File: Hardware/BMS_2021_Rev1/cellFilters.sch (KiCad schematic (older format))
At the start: 14 parts

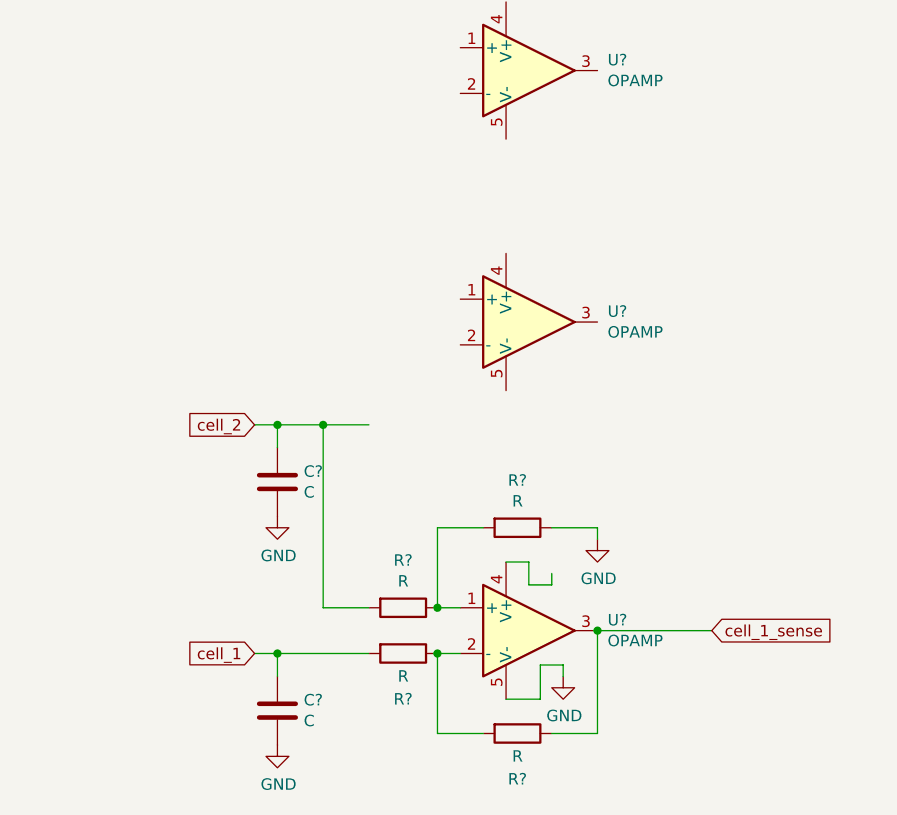
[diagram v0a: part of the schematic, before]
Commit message: Cell filter design finished
need to add resistor values. diodes?
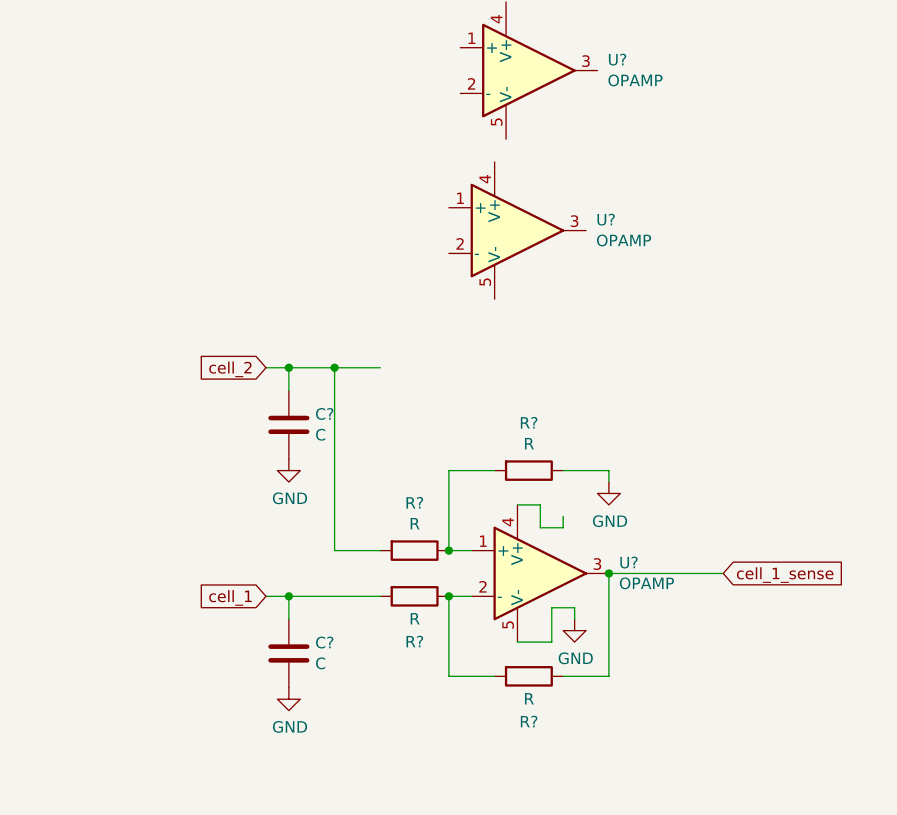
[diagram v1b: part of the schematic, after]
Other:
- moved on the sheet: C?, R?, U?
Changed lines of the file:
@@
 $Descr A4 11693 8268
 encoding utf-8
-Sheet 2 2
+Sheet 2 3
 Title ""
 Date ""
@@
 L pspice:OPAMP U?
 U 1 1 5F757117
-P 8600 4450
-F 0 "U?" H 8944 4496 50  0000 L CNN
-F 1 "OPAMP" H 8944 4405 50  0000 L CNN
-F 2 "" H 8600 4450 50  0001 C CNN
-F 3 "~" H 8600 4450 50  0001 C CNN
-	1    8600 4450
+P 8550 4050
+F 0 "U?" H 8894 4096 50  0000 L CNN
+F 1 "OPAMP" H 8894 4005 50  0000 L CNN
+F 2 "" H 8550 4050 50  0001 C CNN
+F 3 "~" H 8550 4050 50  0001 C CNN
+	1    8550 4050
 	1    0    0    -1
 $EndComp
@@
 L pspice:OPAMP U?
 U 1 1 5F75711D
-P 8600 5800
-F 0 "U?" H 8944 5846 50  0000 L CNN
-F 1 "OPAMP" H 8944 5755 50  0000 L CNN
-F 2 "" H 8600 5800 50  0001 C CNN
-F 3 "~" H 8600 5800 50  0001 C CNN
-	1    8600 5800
-	1    0    0    -1
-$EndComp
-Text GLabel 7400 5900 0    50   Input ~ 0
+P 8650 5550
+F 0 "U?" H 8994 5596 50  0000 L CNN
+F 1 "OPAMP" H 8994 5505 50  0000 L CNN
+F 2 "" H 8650 5550 50  0001 C CNN
+F 3 "~" H 8650 5550 50  0001 C CNN
+	1    8650 5550
+	1    0    0    -1
+$EndComp
+Text GLabel 7450 5650 0    50   Input ~ 0
 cell_1
 $Comp
 L Device:C C?
 U 1 1 5F76C0D8
-P 7500 6150
-F 0 "C?" H 7615 6196 50  0000 L CNN
-F 1 "C" H 7615 6105 50  0000 L CNN
-F 2 "" H 7538 6000 50  0001 C CNN
-F 3 "~" H 7500 6150 50  0001 C CNN
-	1    7500 6150
+P 7550 5900
+F 0 "C?" H 7665 5946 50  0000 L CNN
+F 1 "C" H 7665 5855 50  0000 L CNN
+F 2 "" H 7588 5750 50  0001 C CNN
+F 3 "~" H 7550 5900 50  0001 C CNN
+	1    7550 5900
 	1    0    0    -1
 $EndComp
@@
 L Device:R R?
 U 1 1 5F76C9A3
-P 8050 5900
-F 0 "R?" V 8250 5900 50  0000 C CNN
-F 1 "R" V 8150 5900 50  0000 C CNN
-F 2 "" V 7980 5900 50  0001 C CNN
-F 3 "~" H 8050 5900 50  0001 C CNN
-	1    8050 5900
-	0    1    1    0
-$EndComp
-Wire Wire Line
-	7400 5900 7500 5900
-Wire Wire Line
-	7500 5900 7500 6000
-Wire Wire Line
-	7500 5900 7900 5900
-Connection ~ 7500 5900
-Wire Wire Line
-	8200 5900 8300 5900
-Wire Wire Line
-	8200 5900 8200 6250
-Wire Wire Line
-	8200 6250 8400 6250
-Wire Wire Line
-	8900 6250 8900 5800
-Connection ~ 8200 5900
-Wire Wire Line
-	8900 5800 9400 5800
+P 8100 5650
+F 0 "R?" V 8300 5650 50  0000 C CNN
+F 1 "R" V 8200 5650 50  0000 C CNN
+F 2 "" V 8030 5650 50  0001 C CNN
+F 3 "~" H 8100 5650 50  0001 C CNN
+	1    8100 5650
+	0    1    1    0
+$EndComp
+Wire Wire Line
+	7450 5650 7550 5650
+Wire Wire Line
+	7550 5650 7550 5750
+Wire Wire Line
+	7550 5650 7950 5650
+Connection ~ 7550 5650
+Wire Wire Line
+	8250 5650 8350 5650
+Wire Wire Line
+	8250 5650 8250 6000
+Wire Wire Line
+	8250 6000 8450 6000
+Wire Wire Line
+	8950 6000 8950 5550
+Connection ~ 8250 5650
+Wire Wire Line
+	8950 5550 9450 5550
 $Comp
 L Device:R R?
 U 1 1 5F76FD0D
-P 8550 6250
-F 0 "R?" V 8750 6250 50  0000 C CNN
-F 1 "R" V 8650 6250 50  0000 C CNN
-F 2 "" V 8480 6250 50  0001 C CNN
-F 3 "~" H 8550 6250 50  0001 C CNN
-	1    8550 6250
-	0    1    1    0
-$EndComp
-Wire Wire Line
-	8700 6250 8900 6250
+P 8600 6000
+F 0 "R?" V 8800 6000 50  0000 C CNN
+F 1 "R" V 8700 6000 50  0000 C CNN
+F 2 "" V 8530 6000 50  0001 C CNN
+F 3 "~" H 8600 6000 50  0001 C CNN
+	1    8600 6000
+	0    1    1    0
+$EndComp
+Wire Wire Line
+	8750 6000 8950 6000
 $Comp
 L Device:R R?
 U 1 1 5F770319
-P 8050 5700
-F 0 "R?" V 7843 5700 50  0000 C CNN
-F 1 "R" V 7934 5700 50  0000 C CNN
-F 2 "" V 7980 5700 50  0001 C CNN
-F 3 "~" H 8050 5700 50  0001 C CNN
-	1    8050 5700
-	0    1    1    0
-$EndComp
-Connection ~ 8900 5800
-Wire Wire Line
-	8500 6100 8650 6100
-Wire Wire Line
-	8650 6100 8650 5950
-Wire Wire Line
-	8650 5950 8750 5950
-Wire Wire Line
-	8750 5950 8750 6000
+P 8100 5450
+F 0 "R?" V 7893 5450 50  0000 C CNN
+F 1 "R" V 7984 5450 50  0000 C CNN
+F 2 "" V 8030 5450 50  0001 C CNN
+F 3 "~" H 8100 5450 50  0001 C CNN
+	1    8100 5450
+	0    1    1    0
+$EndComp
+Connection ~ 8950 5550
+Wire Wire Line
+	8550 5850 8700 5850
+Wire Wire Line
+	8700 5850 8700 5700
+Wire Wire Line
+	8700 5700 8800 5700
+Wire Wire Line
+	8800 5700 8800 5750
 $Comp
 L power:GND #PWR?
 U 1 1 5F77381F
-P 8750 6000
-F 0 "#PWR?" H 8750 5750 50  0001 C CNN
-F 1 "GND" H 8755 5827 50  0000 C CNN
-F 2 "" H 8750 6000 50  0001 C CNN
-F 3 "" H 8750 6000 50  0001 C CNN
-	1    8750 6000
-	1    0    0    -1
-$EndComp
-Wire Wire Line
-	8200 5700 8300 5700
-Wire Wire Line
-	8200 5700 8200 5350
-Wire Wire Line
-	8200 5350 8400 5350
-Wire Wire Line
-	8900 5350 8900 5400
-Connection ~ 8200 5700
+P 8800 5750
+F 0 "#PWR?" H 8800 5500 50  0001 C CNN
+F 1 "GND" H 8805 5577 50  0000 C CNN
+F 2 "" H 8800 5750 50  0001 C CNN
+F 3 "" H 8800 5750 50  0001 C CNN
+	1    8800 5750
+	1    0    0    -1
+$EndComp
+Wire Wire Line
+	8250 5450 8350 5450
+Wire Wire Line
+	8250 5450 8250 5100
+Wire Wire Line
+	8250 5100 8450 5100
+Wire Wire Line
+	8950 5100 8950 5150
+Connection ~ 8250 5450
 $Comp
 L power:GND #PWR?
 U 1 1 5F774588
-P 8900 5400
-F 0 "#PWR?" H 8900 5150 50  0001 C CNN
-F 1 "GND" H 8905 5227 50  0000 C CNN
-F 2 "" H 8900 5400 50  0001 C CNN
-F 3 "" H 8900 5400 50  0001 C CNN
-	1    8900 5400
+P 8950 5150
+F 0 "#PWR?" H 8950 4900 50  0001 C CNN
+F 1 "GND" H 8955 4977 50  0000 C CNN
+F 2 "" H 8950 5150 50  0001 C CNN
+F 3 "" H 8950 5150 50  0001 C CNN
+	1    8950 5150
 	1    0    0    -1
 $EndComp
@@
 L Device:R R?
 U 1 1 5F774DFD
-P 8550 5350
-F 0 "R?" V 8343 5350 50  0000 C CNN
-F 1 "R" V 8434 5350 50  0000 C CNN
-F 2 "" V 8480 5350 50  0001 C CNN
-F 3 "~" H 8550 5350 50  0001 C CNN
-	1    8550 5350
-	0    1    1    0
-$EndComp
-Wire Wire Line
-	8700 5350 8900 5350
-Wire Wire Line
-	8500 5500 8600 5500
-Wire Wire Line
-	8600 5500 8600 5600
-Wire Wire Line
-	8600 5600 8700 5600
-Wire Wire Line
-	8700 5600 8700 5550
-Text GLabel 7400 4900 0    50   Input ~ 0
+P 8600 5100
+F 0 "R?" V 8393 5100 50  0000 C CNN
+F 1 "R" V 8484 5100 50  0000 C CNN
+F 2 "" V 8530 5100 50  0001 C CNN
+F 3 "~" H 8600 5100 50  0001 C CNN
+	1    8600 5100
+	0    1    1    0
+$EndComp
+Wire Wire Line
+	8750 5100 8950 5100
+Wire Wire Line
+	8550 5250 8650 5250
+Wire Wire Line
+	8650 5250 8650 5350
+Wire Wire Line
+	8650 5350 8750 5350
+Wire Wire Line
+	8750 5350 8750 5300
+Text GLabel 7450 4650 0    50   Input ~ 0
 cell_2
 Wire Wire Line
-	7400 4900 7500 4900
-Wire Wire Line
-	7500 4900 7500 5000
-Wire Wire Line
-	7500 4900 7700 4900
-Connection ~ 7500 4900
-Wire Wire Line
-	7700 4900 7700 5700
-Wire Wire Line
-	7700 5700 7900 5700
-Connection ~ 7700 4900
-Wire Wire Line
-	7700 4900 7900 4900
+	7450 4650 7550 4650
+Wire Wire Line
+	7550 4650 7550 4750
+Wire Wire Line
+	7550 4650 7750 4650
+Connection ~ 7550 4650
+Wire Wire Line
+	7750 4650 7750 5450
+Wire Wire Line
+	7750 5450 7950 5450
+Connection ~ 7750 4650
+Wire Wire Line
+	7750 4650 7950 4650
 $Comp
 L Device:C C?
 U 1 1 5F777411
-P 7500 5150
-F 0 "C?" H 7615 5196 50  0000 L CNN
-F 1 "C" H 7615 5105 50  0000 L CNN
-F 2 "" H 7538 5000 50  0001 C CNN
-F 3 "~" H 7500 5150 50  0001 C CNN
-	1    7500 5150
+P 7550 4900
+F 0 "C?" H 7665 4946 50  0000 L CNN
+F 1 "C" H 7665 4855 50  0000 L CNN
+F 2 "" H 7588 4750 50  0001 C CNN
+F 3 "~" H 7550 4900 50  0001 C CNN
+	1    7550 4900
 	1    0    0    -1
 $EndComp
@@
 L power:GND #PWR?
 U 1 1 5F77794D
-P 7500 5300
-F 0 "#PWR?" H 7500 5050 50  0001 C CNN
-F 1 "GND" H 7505 5127 50  0000 C CNN
-F 2 "" H 7500 5300 50  0001 C CNN
-F 3 "" H 7500 5300 50  0001 C CNN
-	1    7500 5300
+P 7550 5050
+F 0 "#PWR?" H 7550 4800 50  0001 C CNN
+F 1 "GND" H 7555 4877 50  0000 C CNN
+F 2 "" H 7550 5050 50  0001 C CNN
+F 3 "" H 7550 5050 50  0001 C CNN
+	1    7550 5050
 	1    0    0    -1
 $EndComp
@@
 L power:GND #PWR?
 U 1 1 5F77845A
-P 7500 6300
-F 0 "#PWR?" H 7500 6050 50  0001 C CNN
-F 1 "GND" H 7505 6127 50  0000 C CNN
-F 2 "" H 7500 6300 50  0001 C CNN
-F 3 "" H 7500 6300 50  0001 C CNN
-	1    7500 6300
-	1    0    0    -1
-$EndComp
-Text GLabel 9400 5800 2    50   Input ~ 0
+P 7550 6050
+F 0 "#PWR?" H 7550 5800 50  0001 C CNN
+F 1 "GND" H 7555 5877 50  0000 C CNN
+F 2 "" H 7550 6050 50  0001 C CNN
+F 3 "" H 7550 6050 50  0001 C CNN
+	1    7550 6050
+	1    0    0    -1
+$EndComp
+Text GLabel 9450 5550 2    50   Input ~ 0
 cell_1_sense
 $EndSCHEMATC
